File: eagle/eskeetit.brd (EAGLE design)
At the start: 47 x 28 mm, 46 parts, among them M1 WIRELESS-NRF24L01, U1 GY-521MPU6050, U2 TPS63000DRCR, Y1 20MHz

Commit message: fixed changes in the remote design review
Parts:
- moved C2 2.07 mm to (9.22, 23.7), turned to 180 degrees
- moved C1 1.35 mm to (9.44, 25.8), turned to 180 degrees
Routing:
- net GND: track 32.8 -> 42.7 mm, vias 10 -> 11
- net SWDIO: track 28.4 -> 34.9 mm
- net 3.3V: track 56.0 -> 49.5 mm

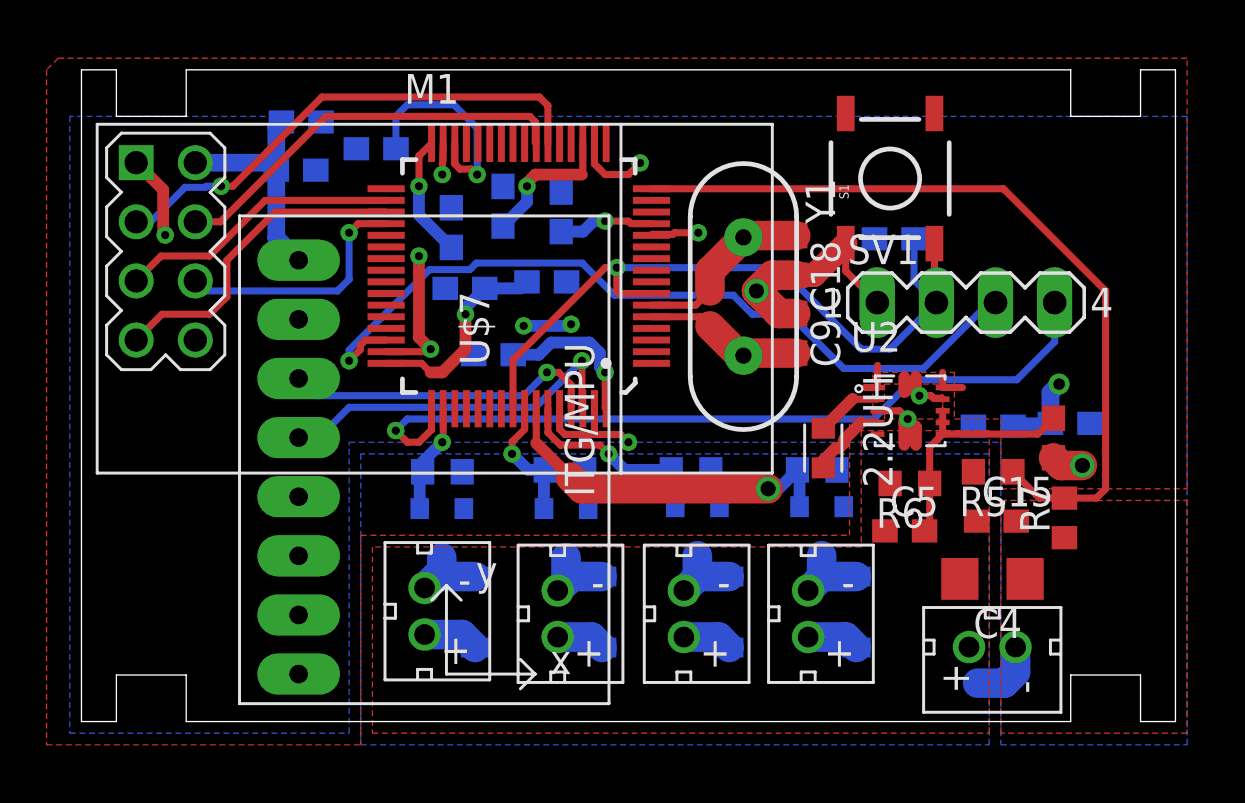
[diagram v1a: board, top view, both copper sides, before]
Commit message: moved capacitors near the JST Connectors
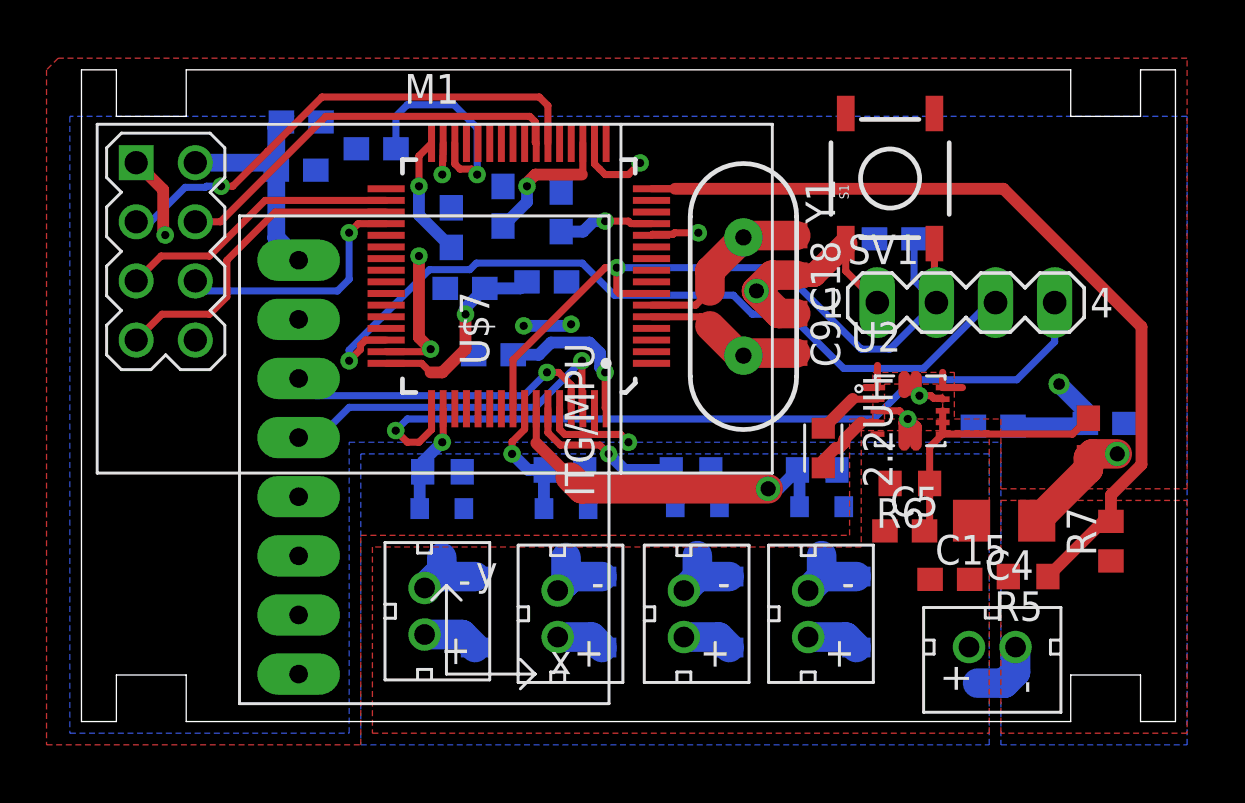
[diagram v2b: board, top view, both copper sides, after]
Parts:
- moved R5 4.74 mm to (40.7, 6.23)
- moved C15 3.20 mm to (37.3, 6.11)
- moved C4 2.55 mm to (39.6, 8.63)
- moved R7 2.24 mm to (44.2, 7.75)
- moved C13 1.50 mm to (43.3, 12.2)
- moved C7 1.50 mm to (44.0, 12.8)
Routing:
- net GND: track 42.7 -> 46.2 mm
- net 3.3V: track 49.5 -> 51.3 mm
- net PA5: track 34.4 -> 36.1 mm
- net N$3: track 10.5 -> 12.0 mm
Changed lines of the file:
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@@
 <attribute name="VALUE" x="8.805" y="27.665" size="1.27" layer="28" rot="MR180"/>
 </element>
-<element name="C13" library="capstone" package="RCL_C0603" value="100nF" x="41.76" y="12.18" smashed="yes" rot="R270">
-<attribute name="SPICEPREFIX" value="C" x="-6.5" y="-31" size="1.778" layer="27" rot="R270" display="off"/>
+<element name="C13" library="capstone" package="RCL_C0603" value="100nF" x="43.26" y="12.18" smashed="yes" rot="R270">
+<attribute name="SPICEPREFIX" value="C" x="-5" y="-31" size="1.778" layer="27" rot="R270" display="off"/>
 </element>
 <element name="C14" library="capstone" package="RCL_C0603" value="4.7uF" x="12.66" y="24.61" smashed="yes" rot="MR0">
@@
 <attribute name="VALUE" x="13.295" y="22.705" size="1.27" layer="28" rot="MR0"/>
 </element>
-<element name="C15" library="capstone" package="RCL_C0603" value="4.7uF" x="39.31" y="8.61" smashed="yes">
-<attribute name="NAME" x="38.675" y="9.245" size="1.27" layer="25"/>
-<attribute name="SPICEPREFIX" value="C" x="99" y="-46" size="1.778" layer="27" display="off"/>
-<attribute name="VALUE" x="38.675" y="6.705" size="1.27" layer="27"/>
+<element name="C15" library="capstone" package="RCL_C0603" value="4.7uF" x="37.31" y="6.11" smashed="yes">
+<attribute name="NAME" x="36.675" y="6.745" size="1.27" layer="25"/>
+<attribute name="SPICEPREFIX" value="C" x="97" y="-48.5" size="1.778" layer="27" display="off"/>
+<attribute name="VALUE" x="36.675" y="4.205" size="1.27" layer="27"/>
 </element>
 <element name="C16" library="capstone" package="RCL_C0603" value="100nF" x="17.7" y="15.76" smashed="yes" rot="MR0">
@@
 <attribute name="VALUE" x="19.355" y="20.795" size="1.27" layer="28" rot="MR180"/>
 </element>
-<element name="C4" library="rcl" library_urn="urn:adsk.eagle:library:334" package="C1206" package3d_urn="urn:adsk.eagle:package:23618/2" value="100uF" x="39.14" y="6.13" smashed="yes" rot="R180">
-<attribute name="NAME" x="40.41" y="4.86" size="1.27" layer="25" rot="R180"/>
-<attribute name="SPICEPREFIX" value="C" x="-1.5" y="45.5" size="1.778" layer="27" rot="R180" display="off"/>
-<attribute name="VALUE" x="40.41" y="8.67" size="1.27" layer="27" rot="R180"/>
+<element name="C4" library="rcl" library_urn="urn:adsk.eagle:library:334" package="C1206" package3d_urn="urn:adsk.eagle:package:23618/2" value="100uF" x="39.64" y="8.63" smashed="yes" rot="R180">
+<attribute name="NAME" x="40.91" y="7.36" size="1.27" layer="25" rot="R180"/>
+<attribute name="SPICEPREFIX" value="C" x="-1" y="48" size="1.778" layer="27" rot="R180" display="off"/>
+<attribute name="VALUE" x="40.91" y="11.17" size="1.27" layer="27" rot="R180"/>
 </element>
 <element name="C5" library="capstone" package="RCL_C0603" value="10uF" x="35.37" y="8.19" smashed="yes">
@@
 <attribute name="VALUE" x="34.735" y="6.285" size="1.27" layer="27"/>
 </element>
-<element name="C7" library="capstone" package="RCL_C0603" value="10uF" x="42.48" y="12.81" smashed="yes" rot="MR180">
-<attribute name="NAME" x="41.845" y="12.175" size="1.27" layer="26" rot="MR180"/>
-<attribute name="SPICEPREFIX" value="C" x="72.96" y="72.5" size="1.778" layer="28" rot="MR180" display="off"/>
+<element name="C7" library="capstone" package="RCL_C0603" value="10uF" x="43.98" y="12.81" smashed="yes" rot="MR180">
+<attribute name="NAME" x="43.345" y="12.175" size="1.27" layer="26" rot="MR180"/>
+<attribute name="SPICEPREFIX" value="C" x="74.46" y="72.5" size="1.778" layer="28" rot="MR180" display="off"/>
 </element>
 <element name="C8" library="capstone" package="RCL_C0603" value="10uF" x="39.17" y="12.69" smashed="yes" rot="MR0">
@@
 <attribute name="VALUE" x="14.875" y="12.635" size="1.27" layer="28" rot="MR180"/>
 </element>
-<element name="R5" library="rcl" library_urn="urn:adsk.eagle:library:334" package="R0603" package3d_urn="urn:adsk.eagle:package:23555/2" value="20k" x="39.17" y="10.73" smashed="yes" rot="R180">
-<attribute name="NAME" x="39.805" y="10.095" size="1.27" layer="25" rot="R180"/>
-<attribute name="SPICEPREFIX" value="R" x="12.5" y="75.5" size="1.778" layer="27" rot="R180" display="off"/>
+<element name="R5" library="rcl" library_urn="urn:adsk.eagle:library:334" package="R0603" package3d_urn="urn:adsk.eagle:package:23555/2" value="20k" x="40.67" y="6.23" smashed="yes" rot="R180">
+<attribute name="NAME" x="41.305" y="5.595" size="1.27" layer="25" rot="R180"/>
+<attribute name="SPICEPREFIX" value="R" x="14" y="71" size="1.778" layer="27" rot="R180" display="off"/>
 </element>
 <element name="R6" library="rcl" library_urn="urn:adsk.eagle:library:334" package="R0603" package3d_urn="urn:adsk.eagle:package:23555/2" value="100" x="35.59" y="10.23" smashed="yes" rot="R180">
@@
 <attribute name="VALUE" x="36.225" y="12.135" size="1.27" layer="27" rot="R180"/>
 </element>
-<element name="R7" library="rcl" library_urn="urn:adsk.eagle:library:334" package="R0603" package3d_urn="urn:adsk.eagle:package:23555/2" value="20k" x="42.23" y="8.75" smashed="yes" rot="R90">
-<attribute name="NAME" x="41.595" y="8.115" size="1.27" layer="25" rot="R90"/>
-<attribute name="SPICEPREFIX" value="R" x="107" y="40.5" size="1.778" layer="27" rot="R90" display="off"/>
-<attribute name="VALUE" x="44.135" y="8.115" size="1.27" layer="27" rot="R90"/>
+<element name="R7" library="rcl" library_urn="urn:adsk.eagle:library:334" package="R0603" package3d_urn="urn:adsk.eagle:package:23555/2" value="20k" x="44.23" y="7.75" smashed="yes" rot="R90">
+<attribute name="NAME" x="43.595" y="7.115" size="1.27" layer="25" rot="R90"/>
+<attribute name="SPICEPREFIX" value="R" x="109" y="39.5" size="1.778" layer="27" rot="R90" display="off"/>
+<attribute name="VALUE" x="46.135" y="7.115" size="1.27" layer="27" rot="R90"/>
 </element>
 <element name="S1" library="Aircopter_quad_lib" package="TACTILE-SWITCH-SMD" value="SWITCH-MOMENTARY-2SMD" x="34.74" y="23.33" smashed="yes" rot="R90">
@@
 <wire x1="14.89" y1="15.89" x2="15" y2="16" width="0.3048" layer="1"/>
 <via x="15" y="16" extent="1-16" drill="0.35"/>
-<wire x1="41.76" y1="11.33" x2="42.09" y2="11" width="1.27" layer="1"/>
-<via x="43" y="11" extent="1-16" drill="0.65"/>
-<wire x1="42.09" y1="11" x2="43" y2="11" width="1.27" layer="1"/>
+<via x="44.5" y="11.5" extent="1-16" drill="0.65"/>
+<wire x1="44.5" y1="11.5" x2="43.43" y2="11.5" width="1.27" layer="1"/>
+<wire x1="43.26" y1="11.33" x2="43.43" y2="11.5" width="1.27" layer="1"/>
 <wire x1="23.1648" y1="12.3352" x2="23.5" y2="12" width="0.3048" layer="1"/>
 <via x="23.5" y="12" extent="1-16" drill="0.35"/>
@@
 <wire x1="35.35" y1="14.8" x2="35.35" y2="14.15" width="0.508" layer="1"/>
 <wire x1="35.85" y1="14.8" x2="35.85" y2="14.15" width="0.508" layer="1"/>
+<wire x1="43.26" y1="11.33" x2="43.26" y2="10.85" width="1.27" layer="1"/>
+<wire x1="43.26" y1="10.85" x2="41.04" y2="8.63" width="1.27" layer="1"/>
 </signal>
 <signal name="MOTOR2_PWM">
@@
 <contactref element="C2" pad="1"/>
 <contactref element="U1" pad="VCC"/>
-<wire x1="42" y1="14.5" x2="41.63" y2="14.13" width="0.762" layer="16"/>
 <via x="42" y="14.5" extent="1-16" drill="0.5"/>
-<wire x1="41.63" y1="14.13" x2="41.63" y2="12.81" width="0.762" layer="16"/>
-<wire x1="40.02" y1="12.69" x2="41.51" y2="12.69" width="0.762" layer="16"/>
-<wire x1="41.51" y1="12.69" x2="41.63" y2="12.81" width="0.762" layer="16"/>
+<wire x1="42" y1="14.5" x2="43.13" y2="13.37" width="0.762" layer="16"/>
+<wire x1="43.13" y1="13.37" x2="43.13" y2="12.81" width="0.762" layer="16"/>
+<wire x1="40.02" y1="12.69" x2="43.01" y2="12.69" width="0.762" layer="16"/>
+<wire x1="43.01" y1="12.69" x2="43.13" y2="12.81" width="0.762" layer="16"/>
 <wire x1="20.61" y1="21.05" x2="21.55" y2="21.05" width="0.508" layer="16"/>
 <wire x1="21.55" y1="21.05" x2="22" y2="21.5" width="0.508" layer="16"/>
@@
 <wire x1="15" y1="15" x2="14.61" y2="15.39" width="0.3048" layer="1"/>
 <polygon width="0.1524" layer="1" thermals="no">
-<vertex x="12" y="-0.5"/>
+<vertex x="12" y="-1"/>
 <vertex x="12" y="8"/>
 <vertex x="33" y="8"/>
@@
 <vertex x="-1.5" y="28"/>
 <vertex x="-1.5" y="-1"/>
-<vertex x="12" y="-1"/>
 </polygon>
 <wire x1="34.2" y1="14.35" x2="34.2" y2="15.3" width="0.3048" layer="1"/>
@@
 <wire x1="37" y1="12.85" x2="37" y2="12.35" width="0.3048" layer="1"/>
 <wire x1="37" y1="13.35" x2="37" y2="12.85" width="0.3048" layer="1"/>
-<wire x1="37" y1="12.35" x2="41.08" y2="12.35" width="0.3048" layer="1"/>
-<wire x1="41.08" y1="12.35" x2="41.76" y2="13.03" width="0.3048" layer="1"/>
+<wire x1="37" y1="12.35" x2="42.58" y2="12.35" width="0.3048" layer="1"/>
+<wire x1="42.58" y1="12.35" x2="43.26" y2="13.03" width="0.3048" layer="1"/>
 </signal>
 <signal name="N$4">
@@
 <contactref element="R5" pad="1"/>
 <contactref element="R7" pad="2"/>
-<wire x1="40.02" y1="10.73" x2="41.15" y2="9.6" width="0.3048" layer="1"/>
-<wire x1="41.15" y1="9.6" x2="42.23" y2="9.6" width="0.3048" layer="1"/>
 <contactref element="U$7" pad="16"/>
-<wire x1="24.49" y1="22.89" x2="39.61" y2="22.89" width="0.3048" layer="1"/>
-<wire x1="39.61" y1="22.89" x2="44" y2="18.5" width="0.3048" layer="1"/>
-<wire x1="44" y1="18.5" x2="44" y2="10" width="0.3048" layer="1"/>
-<wire x1="43.6" y1="9.6" x2="42.23" y2="9.6" width="0.3048" layer="1"/>
-<wire x1="44" y1="10" x2="43.6" y2="9.6" width="0.3048" layer="1"/>
+<wire x1="25.5" y1="22.89" x2="39.61" y2="22.89" width="0.508" layer="1"/>
+<wire x1="39.61" y1="22.89" x2="45.5414" y2="16.9586" width="0.508" layer="1"/>
+<wire x1="45.5414" y1="16.9586" x2="45.5414" y2="11.0414" width="0.508" layer="1"/>
+<wire x1="45.5414" y1="11.0414" x2="44.23" y2="9.73" width="0.508" layer="1"/>
+<wire x1="44.23" y1="9.73" x2="44.23" y2="8.6" width="0.508" layer="1"/>
+<wire x1="44.23" y1="8.6" x2="43.89" y2="8.6" width="0.508" layer="1"/>
+<wire x1="43.89" y1="8.6" x2="41.52" y2="6.23" width="0.508" layer="1"/>
+<wire x1="24.49" y1="22.89" x2="25.5" y2="22.89" width="0.3048" layer="1"/>
 </signal>
 </signals>
